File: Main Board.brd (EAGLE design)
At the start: 37.3 x 95 mm, 55 parts, among them IC1 ATSAMD21G18A-AF, IC2 BMP388, IC3 CAT24C64WI-GT3, IC4 DRV2605, IC6 MIC5219-3.3YM5, IC7 MIC5219-5.0YM5, J1 10118194-0001LF, Q1 BC817-25LT1SMD, Y1 ECS-.327-7-34B-TR

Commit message: 6 pin SH connector instead of two 4 pin SH connectors
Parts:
- removed ESC, TELEM: BM04B-SRSS-TB(LF)(SN), Braedin's Eagle Libraries:BM04B-SRSS-TB(LF)(SN)
- added J2: BM06B-SRSS-TB(LF)(SN), BM06B-SRSS-TB(LF)(SN):BM06BSRSSTBLFSN
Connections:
- net 12V: now also J2.6; no longer TELEM.P$1
- net 5V: now also J2.2; no longer ESC.P$3
- net D12_TO_ESC: now also J2.1; no longer ESC.P$4
- net GND: now also J2.3; no longer ESC.P$2, TELEM.P$4
- net RX0_FROM_ESC: now also J2.5; no longer TELEM.P$2
- net TX1_TO_ESC: now also J2.4; no longer TELEM.P$3
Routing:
- net TX1_TO_ESC: track 29.4 -> 23.8 mm
- net D12_TO_ESC: track 24.5 -> 19.3 mm
- net RX0_FROM_ESC: track 30.4 -> 34.7 mm
- net GND: track 292.8 -> 295.1 mm
- net 5V: track 122.0 -> 119.9 mm
- net 12V: track 29.0 -> 28.1 mm
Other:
- board text added: "GND"
- board text added: "TX"
- board text added: "VIN"
- board text removed: "12V"

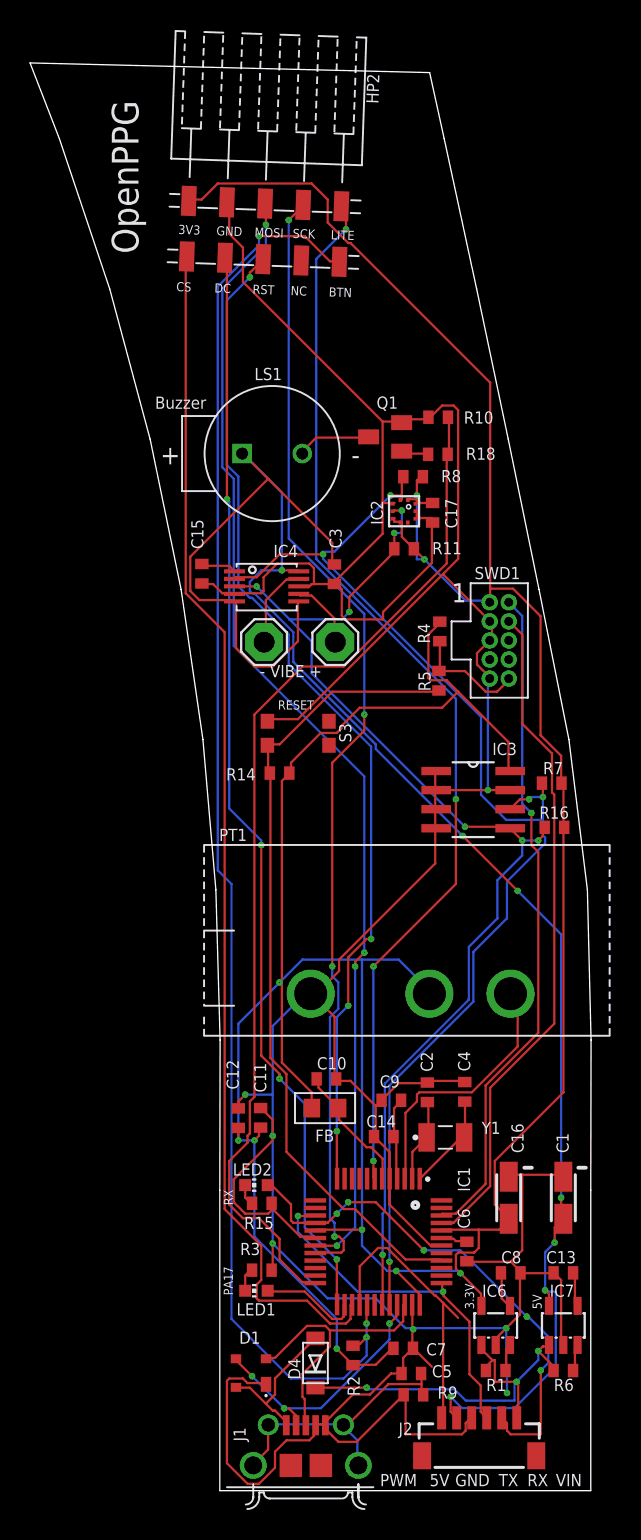
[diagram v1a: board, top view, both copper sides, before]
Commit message: Switching regulator to reduce heat, and added ground planes
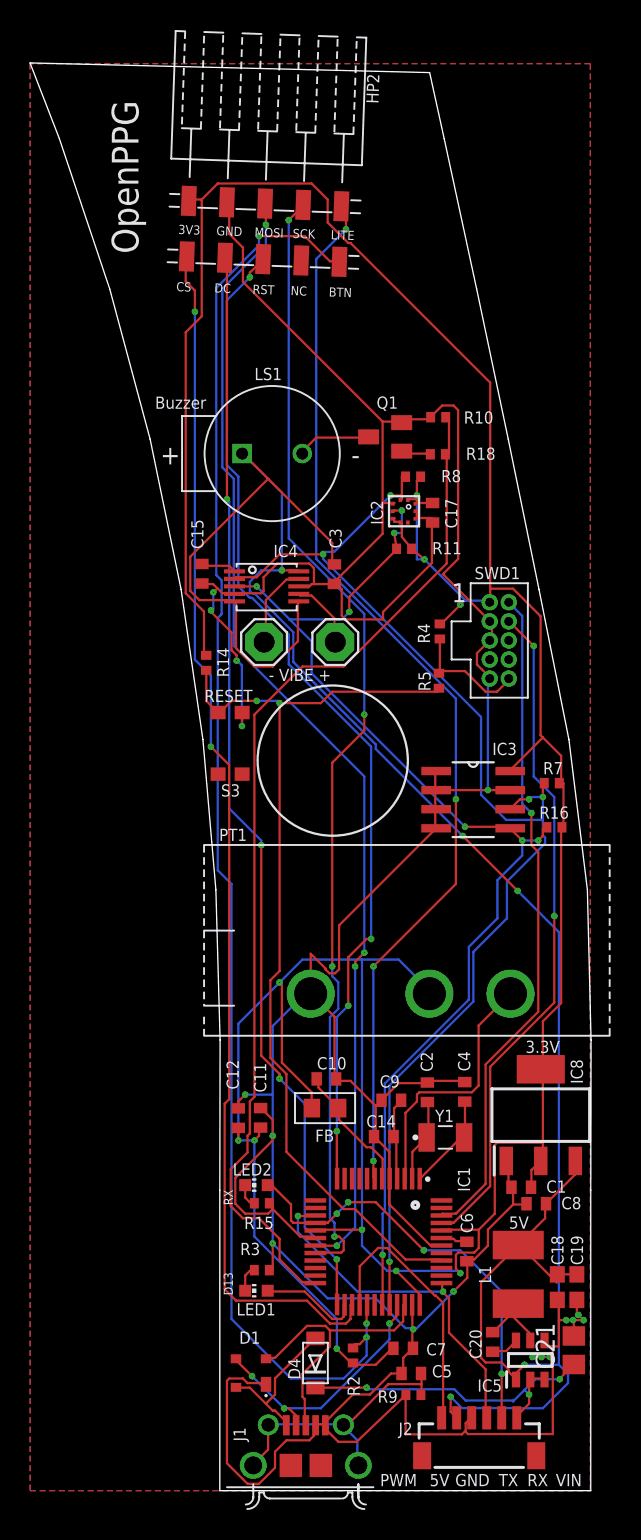
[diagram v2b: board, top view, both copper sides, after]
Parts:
- removed C13: 470pf, rcl:C0402
- removed C16: 2.2uF, adafruit:CT3216
- removed IC6: MIC5219-3.3YM5, v-reg-micrel:SOT23-5
- removed IC7: MIC5219-5.0YM5, v-reg-micrel:SOT23-5
- removed R1, R6: 1k, rcl:R0402
- added C18, C19: 22uf, rcl:C0603
- added C20: 0.1uf, rcl:C0402
- added C21: 10uf, rcl:C0805
- added IC5: AP63205WU-7, AP63205WU-7:SOT95P280X100-6N
- added IC8: AP2114H-3.3TRG1, AP2114H-3.3TRG1:SOT230P700X180-4N
- added L1: 4.7uH, rcl:L1812
- C1: value 2.2uF -> 4.7uf; device adafruit:CT3216 -> rcl:C0402
- C8: value 470pf -> 4.7uf
- moved R14 8.81 mm to (11.7, 55.1), turned to 90 degrees
- moved C8 4.90 mm to (33.7, 19.1), turned to 180 degrees
- moved S3 4.58 mm to (13.3, 49.8), turned to 270 degrees
- moved C1 2.89 mm to (32.7, 20.2), turned to 180 degrees
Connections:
- removed net N$12: C8.1, IC6.4
- removed net N$3: IC6.3, R1.2
- removed net N$5: IC7.3, R6.2
- removed net N$7: C13.1, IC7.4
- new net N$10: C20.2, IC5.5, L1.1
- new net N$11: C20.1, IC5.6
- net 12V: now also C21.1, IC5.2, IC5.3; no longer IC6.1, IC7.1, R1.1, R6.1
- net 3.3V: now also C1.1, IC8.2, IC8.4; no longer C16.+, IC6.5
- net 5V: now also C18.1, C19.1, C8.1, IC5.1, IC8.3, L1.2; no longer C1.+, IC7.5
- net GND: now also C1.2, C18.2, C19.2, C21.2, IC5.4, IC8.1; no longer C1.-, C13.2, C16.-, IC6.2, IC7.2
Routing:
- net 5V: track 119.9 -> 146.9 mm, vias 7 -> 5
- net RST: track 53.8 -> 62.6 mm, vias 0 -> 2
- net RX0_FROM_ESC: track 34.7 -> 28.7 mm, vias 5 -> 4
- net N$10: track 0.00 -> 5.86 mm
- net 12V: track 28.1 -> 23.0 mm
- net GND: track 295.1 -> 291.7 mm, vias 7 -> 17
- net 3.3V: track 248.9 -> 245.7 mm, vias 9 -> 10
- net N$12: track 2.48 -> 0.00 mm
- net N$7: track 2.37 -> 0.00 mm
- net N$11: track 0.00 -> 1.87 mm
- net N$5: track 1.83 -> 0.00 mm
- net N$3: track 1.82 -> 0.00 mm
- net D12_TO_ESC: track 19.3 -> 17.8 mm
- net A0_POT: track 18.2 -> 17.3 mm
- net D10_TFTCS: track 79.7 -> 80.6 mm, vias 0 -> 2
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- added copper zone on layer 1, net GND
- added copper zone on layer 16, net GND
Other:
- board text added: "D13"
- board text removed: "PA17"
